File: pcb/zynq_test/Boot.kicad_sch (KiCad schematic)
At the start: 10 parts, among them J901 A-MicroTF-1.85A, U902 MT25QL01GBBB8ESF-0SIT, U903 TXS02612RTW

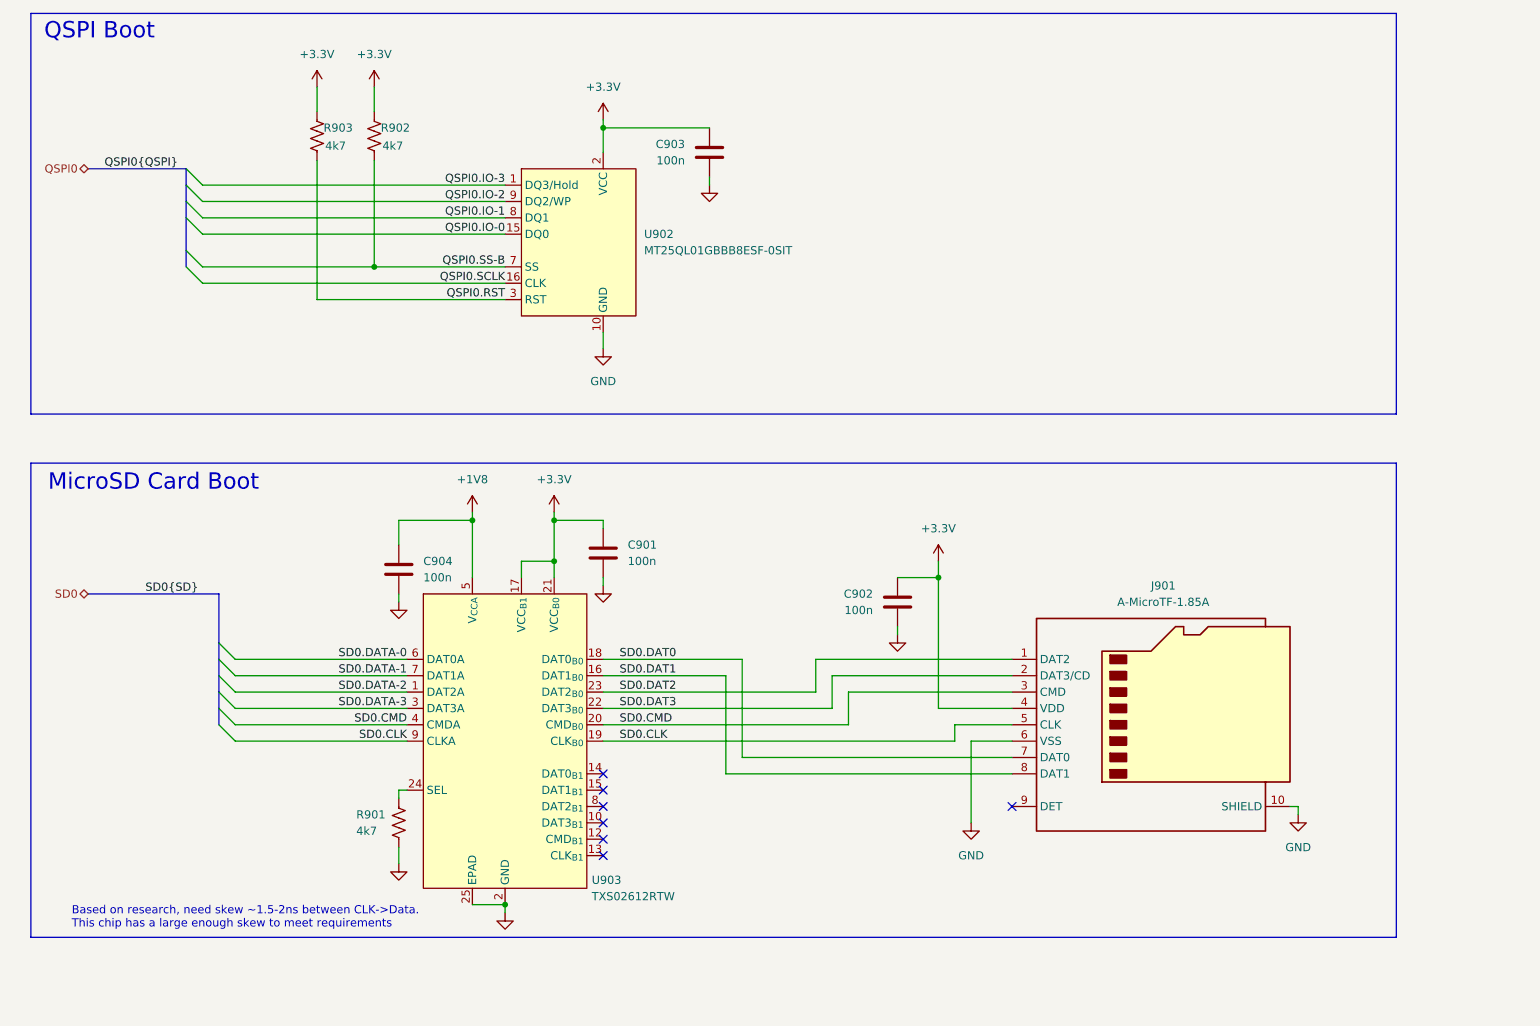
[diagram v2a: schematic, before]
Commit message: Connected DDR3, cleaned up some thing
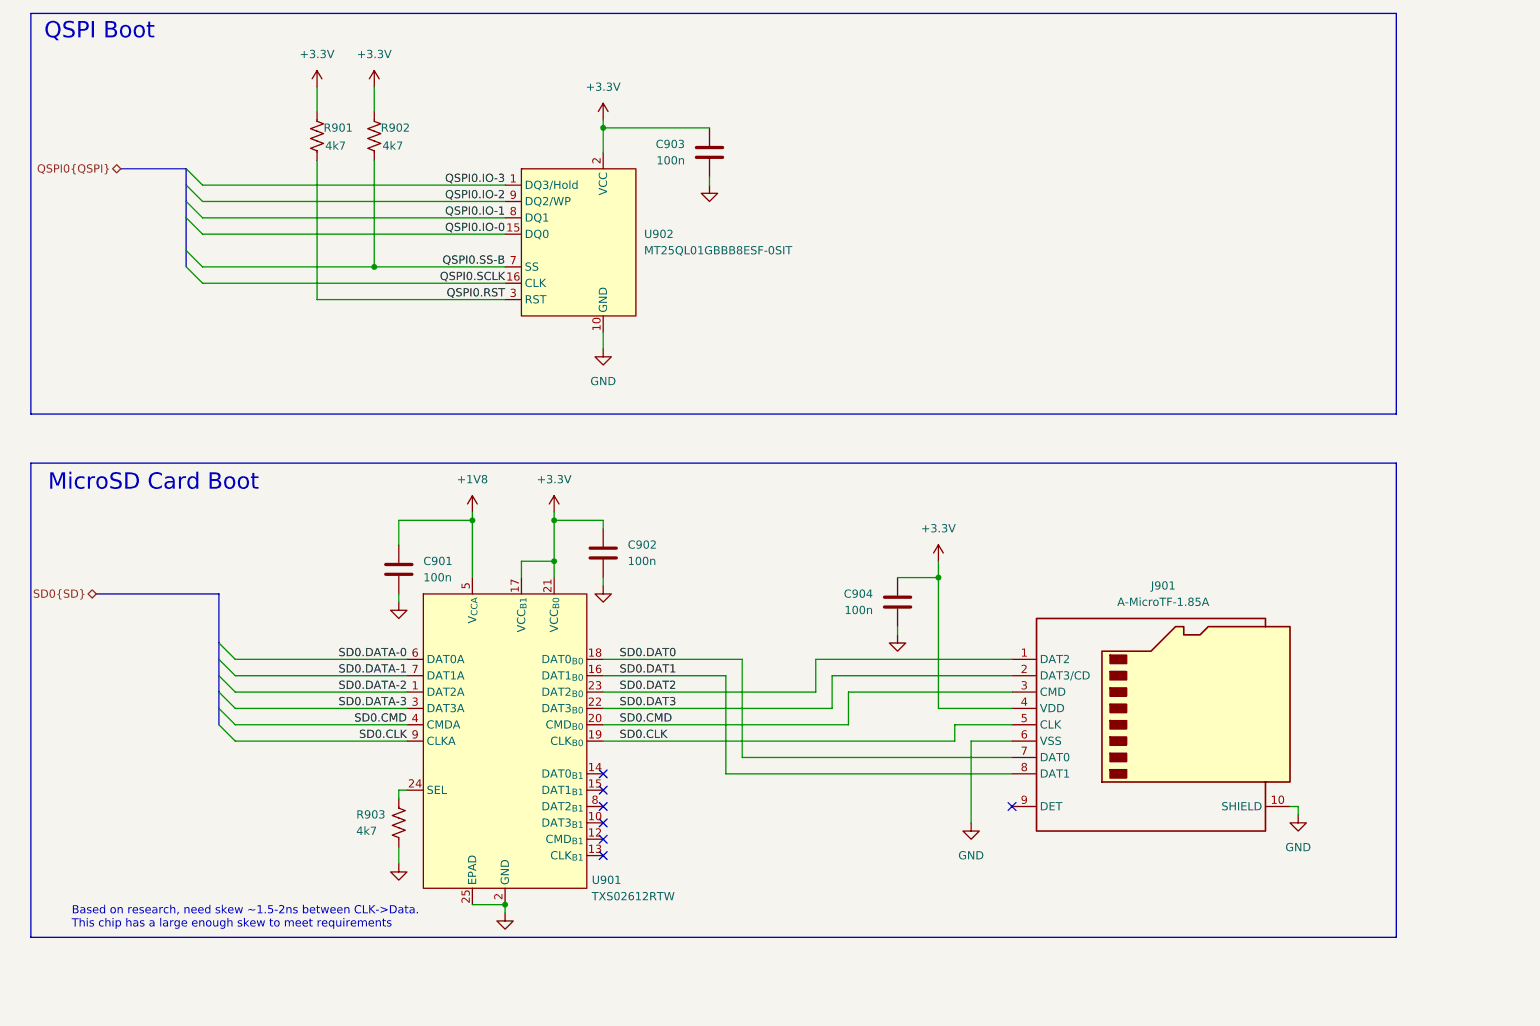
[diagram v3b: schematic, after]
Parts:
- U901: renamed from U903; footprint Package_DFN_QFN:WQFN-24-1EP_4x4mm_P0.5mm_EP2.45x2.45mm -> Package_DFN_QFN:WQFN-24-1EP_4x4mm_P0.5mm_EP2.45x2.45mm_ThermalVias
- renumbered C904 to C901, C901 to C902, C902 to C904, R903 to R901, R901 to R903
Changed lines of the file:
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@@
 	(generator_version "9.0")
 	(paper "A4")
+	(title_block
+		(date "2025-09-06")
+		(rev "v1.0")
+	)
 	(rectangle
 		(start 30.48 21.59)
@@
 	(bus
 		(pts
-			(xy 39.37 45.72) (xy 54.61 45.72)
+			(xy 44.45 45.72) (xy 54.61 45.72)
 		)
 		(stroke
@@
 	(bus
 		(pts
-			(xy 39.37 111.76) (xy 59.69 111.76)
+			(xy 40.64 111.76) (xy 59.69 111.76)
 		)
 		(stroke
@@
 		)
 	)
-	(label "SD0{SD}"
-		(at 48.26 111.76 0)
-		(effects
-			(font
-				(size 1.27 1.27)
-			)
-			(justify left bottom)
-		)
-	)
 	(label "QSPI0.SCLK"
 		(at 104.14 63.5 180)
@@
 		)
 	)
-	(label "QSPI0{QSPI}"
-		(at 41.91 45.72 0)
-		(effects
-			(font
-				(size 1.27 1.27)
-			)
-			(justify left bottom)
-		)
-	)
 	(label "QSPI0.RST"
 		(at 104.14 66.04 180)
@@
 		)
 	)
-	(hierarchical_label "QSPI0"
+	(hierarchical_label "QSPI0{QSPI}"
 		(shape bidirectional)
-		(at 39.37 45.72 180)
+		(at 44.45 45.72 180)
 		(effects
 			(font
@@
 		)
 	)
-	(hierarchical_label "SD0"
+	(hierarchical_label "SD0{SD}"
 		(shape bidirectional)
-		(at 39.37 111.76 180)
+		(at 40.64 111.76 180)
 		(effects
 			(font
@@
 		(dnp no)
 		(fields_autoplaced yes)
-		(property "Reference" "#PWR0912"
+		(property "Reference" "#PWR0901"
 			(at 74.93 36.83 0)
 			(effects
@@
 			(project "zynq_test"
 				(path "/0637578d-4ce5-4d31-b973-2de977269ea5/054c8c8d-10fe-458e-89fa-3861c8d6d3b7"
-					(reference "#PWR0912")
+					(reference "#PWR0901")
 					(unit 1)
 				)
@@
 		(dnp no)
 		(fields_autoplaced yes)
-		(property "Reference" "#PWR0908"
+		(property "Reference" "#PWR0912"
 			(at 165.1 124.46 0)
 			(effects
@@
 			(project "zynq_test"
 				(path "/0637578d-4ce5-4d31-b973-2de977269ea5/054c8c8d-10fe-458e-89fa-3861c8d6d3b7"
-					(reference "#PWR0908")
+					(reference "#PWR0912")
 					(unit 1)
 				)
@@
 		(dnp no)
 		(fields_autoplaced yes)
-		(property "Reference" "#PWR0913"
+		(property "Reference" "#PWR0911"
 			(at 135.89 54.61 0)
 			(effects
@@
 			(project "zynq_test"
 				(path "/0637578d-4ce5-4d31-b973-2de977269ea5/054c8c8d-10fe-458e-89fa-3861c8d6d3b7"
-					(reference "#PWR0913")
+					(reference "#PWR0911")
 					(unit 1)
 				)
@@
 		(on_board yes)
 		(dnp no)
-		(property "Reference" "R903"
+		(property "Reference" "R901"
 			(at 75.946 39.37 0)
 			(effects
@@
 			(project "zynq_test"
 				(path "/0637578d-4ce5-4d31-b973-2de977269ea5/054c8c8d-10fe-458e-89fa-3861c8d6d3b7"
-					(reference "R903")
+					(reference "R901")
 					(unit 1)
 				)
@@
 		(dnp no)
 		(fields_autoplaced yes)
-		(property "Reference" "#PWR0915"
+		(property "Reference" "#PWR0904"
 			(at 87.63 160.02 0)
 			(effects
@@
 			(project "zynq_test"
 				(path "/0637578d-4ce5-4d31-b973-2de977269ea5/054c8c8d-10fe-458e-89fa-3861c8d6d3b7"
-					(reference "#PWR0915")
+					(reference "#PWR0904")
 					(unit 1)
 				)
@@
 		(dnp no)
 		(fields_autoplaced yes)
-		(property "Reference" "#PWR0903"
+		(property "Reference" "#PWR0913"
 			(at 171.45 110.49 0)
 			(effects
@@
 			(project "zynq_test"
 				(path "/0637578d-4ce5-4d31-b973-2de977269ea5/054c8c8d-10fe-458e-89fa-3861c8d6d3b7"
-					(reference "#PWR0903")
+					(reference "#PWR0913")
 					(unit 1)
 				)
@@
 		(dnp no)
 		(fields_autoplaced yes)
-		(property "Reference" "#PWR0906"
+		(property "Reference" "#PWR0903"
 			(at 87.63 119.38 0)
 			(effects
@@
 			(project "zynq_test"
 				(path "/0637578d-4ce5-4d31-b973-2de977269ea5/054c8c8d-10fe-458e-89fa-3861c8d6d3b7"
-					(reference "#PWR0906")
+					(reference "#PWR0903")
 					(unit 1)
 				)
@@
 		(dnp no)
 		(fields_autoplaced yes)
-		(property "Reference" "#PWR0904"
+		(property "Reference" "#PWR0914"
 			(at 176.53 153.67 0)
 			(effects
@@
 			(project "zynq_test"
 				(path "/0637578d-4ce5-4d31-b973-2de977269ea5/054c8c8d-10fe-458e-89fa-3861c8d6d3b7"
-					(reference "#PWR0904")
+					(reference "#PWR0914")
 					(unit 1)
 				)
@@
 		(on_board yes)
 		(dnp no)
-		(property "Reference" "U903"
+		(property "Reference" "U901"
 			(at 117.602 156.21 0)
 			(effects
@@
 			)
 		)
-		(property "Footprint" "Package_DFN_QFN:WQFN-24-1EP_4x4mm_P0.5mm_EP2.45x2.45mm"
+		(property "Footprint" "Package_DFN_QFN:WQFN-24-1EP_4x4mm_P0.5mm_EP2.45x2.45mm_ThermalVias"
 			(at 104.14 170.18 0)
 			(effects
@@
 			(project ""
 				(path "/0637578d-4ce5-4d31-b973-2de977269ea5/054c8c8d-10fe-458e-89fa-3861c8d6d3b7"
-					(reference "U903")
+					(reference "U901")
 					(unit 1)
 				)
@@
 		(on_board yes)
 		(dnp no)
-		(property "Reference" "R901"
+		(property "Reference" "R903"
 			(at 81.026 146.05 0)
 			(effects
@@
 			(project ""
 				(path "/0637578d-4ce5-4d31-b973-2de977269ea5/054c8c8d-10fe-458e-89fa-3861c8d6d3b7"
-					(reference "R901")
+					(reference "R903")
 					(unit 1)
 				)
@@
 		(dnp no)
 		(fields_autoplaced yes)
-		(property "Reference" "C902"
+		(property "Reference" "C904"
 			(at 161.29 111.7599 0)
 			(effects
@@
 			(project "zynq_test"
 				(path "/0637578d-4ce5-4d31-b973-2de977269ea5/054c8c8d-10fe-458e-89fa-3861c8d6d3b7"
-					(reference "C902")
+					(reference "C904")
 					(unit 1)
 				)
@@
 		(dnp no)
 		(fields_autoplaced yes)
-		(property "Reference" "C901"
+		(property "Reference" "C902"
 			(at 123.19 104.1399 0)
 			(effects
@@
 			(project ""
 				(path "/0637578d-4ce5-4d31-b973-2de977269ea5/054c8c8d-10fe-458e-89fa-3861c8d6d3b7"
-					(reference "C901")
+					(reference "C902")
 					(unit 1)
 				)
@@
 		(dnp no)
 		(fields_autoplaced yes)
-		(property "Reference" "#PWR0907"
+		(property "Reference" "#PWR0910"
 			(at 119.38 116.84 0)
 			(effects
@@
 			(project "zynq_test"
 				(path "/0637578d-4ce5-4d31-b973-2de977269ea5/054c8c8d-10fe-458e-89fa-3861c8d6d3b7"
-					(reference "#PWR0907")
+					(reference "#PWR0910")
 					(unit 1)
 				)
@@
 		(dnp no)
 		(fields_autoplaced yes)
-		(property "Reference" "#PWR0910"
+		(property "Reference" "#PWR0902"
 			(at 83.82 36.83 0)
 			(effects
@@
 			(project "zynq_test"
 				(path "/0637578d-4ce5-4d31-b973-2de977269ea5/054c8c8d-10fe-458e-89fa-3861c8d6d3b7"
-					(reference "#PWR0910")
+					(reference "#PWR0902")
 					(unit 1)
 				)
@@
 		(dnp no)
 		(fields_autoplaced yes)
-		(property "Reference" "#PWR0901"
+		(property "Reference" "#PWR0915"
 			(at 227.33 152.4 0)
 			(effects
@@
 			(project ""
 				(path "/0637578d-4ce5-4d31-b973-2de977269ea5/054c8c8d-10fe-458e-89fa-3861c8d6d3b7"
-					(reference "#PWR0901")
+					(reference "#PWR0915")
 					(unit 1)
 				)
@@
 		(dnp no)
 		(fields_autoplaced yes)
-		(property "Reference" "#PWR0909"
+		(property "Reference" "#PWR0908"
 			(at 119.38 41.91 0)
 			(effects
@@
 			(project "zynq_test"
 				(path "/0637578d-4ce5-4d31-b973-2de977269ea5/054c8c8d-10fe-458e-89fa-3861c8d6d3b7"
-					(reference "#PWR0909")
+					(reference "#PWR0908")
 					(unit 1)
 				)
@@
 		(dnp no)
 		(fields_autoplaced yes)
-		(property "Reference" "C904"
+		(property "Reference" "C901"
 			(at 91.44 106.6799 0)
 			(effects
@@
 			(project "zynq_test"
 				(path "/0637578d-4ce5-4d31-b973-2de977269ea5/054c8c8d-10fe-458e-89fa-3861c8d6d3b7"
-					(reference "C904")
+					(reference "C901")
 					(unit 1)
 				)
@@
 		(dnp no)
 		(fields_autoplaced yes)
-		(property "Reference" "#PWR0902"
+		(property "Reference" "#PWR0907"
 			(at 111.76 102.87 0)
 			(effects
@@
 			(project ""
 				(path "/0637578d-4ce5-4d31-b973-2de977269ea5/054c8c8d-10fe-458e-89fa-3861c8d6d3b7"
-					(reference "#PWR0902")
+					(reference "#PWR0907")
 					(unit 1)
 				)
@@
 		(dnp no)
 		(fields_autoplaced yes)
-		(property "Reference" "#PWR0911"
+		(property "Reference" "#PWR0909"
 			(at 119.38 80.01 0)
 			(effects
@@
 			(project "zynq_test"
 				(path "/0637578d-4ce5-4d31-b973-2de977269ea5/054c8c8d-10fe-458e-89fa-3861c8d6d3b7"
-					(reference "#PWR0911")
+					(reference "#PWR0909")
 					(unit 1)
 				)
@@
 		(dnp no)
 		(fields_autoplaced yes)
-		(property "Reference" "#PWR0914"
+		(property "Reference" "#PWR0906"
 			(at 104.14 167.64 0)
 			(effects
@@
 			(project "zynq_test"
 				(path "/0637578d-4ce5-4d31-b973-2de977269ea5/054c8c8d-10fe-458e-89fa-3861c8d6d3b7"
-					(reference "#PWR0914")
+					(reference "#PWR0906")
 					(unit 1)
 				)

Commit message: Finished Power Supply
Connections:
- net +3.3V renamed +3V3
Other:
- title: (none) -> Boot
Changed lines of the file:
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@@
 	(paper "A4")
 	(title_block
-		(date "2025-09-06")
-		(rev "v1.0")
+		(title "Boot")
+		(date "2025-09-13")
+		(rev "A")
 	)
 	(rectangle
@@
 			)
 		)
-		(property "Value" "+3.3V"
+		(property "Value" "+3V3"
 			(at 74.93 27.94 0)
 			(effects
@@
 			)
 		)
-		(property "Value" "+3.3V"
+		(property "Value" "+3V3"
 			(at 171.45 101.6 0)
 			(effects
@@
 			)
 		)
-		(property "Value" "+3.3V"
+		(property "Value" "+3V3"
 			(at 83.82 27.94 0)
 			(effects
@@
 			)
 		)
-		(property "Value" "+3.3V"
+		(property "Value" "+3V3"
 			(at 119.38 33.02 0)
 			(effects
@@
 			)
 		)
-		(property "Value" "+3.3V"
+		(property "Value" "+3V3"
 			(at 111.76 93.98 0)
 			(effects

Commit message: Finished most of the schematic, will start routing soon
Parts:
- U901: footprint Package_DFN_QFN:WQFN-24-1EP_4x4mm_P0.5mm_EP2.45x2.45mm_ThermalVias -> Package_DFN_QFN:WQFN-24-1EP_4x4mm_P0.5mm_EP2.45x2.45mm
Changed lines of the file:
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@@
 			)
 		)
-		(property "Footprint" "Package_DFN_QFN:WQFN-24-1EP_4x4mm_P0.5mm_EP2.45x2.45mm_ThermalVias"
+		(property "Footprint" "Package_DFN_QFN:WQFN-24-1EP_4x4mm_P0.5mm_EP2.45x2.45mm"
 			(at 104.14 170.18 0)
 			(effects

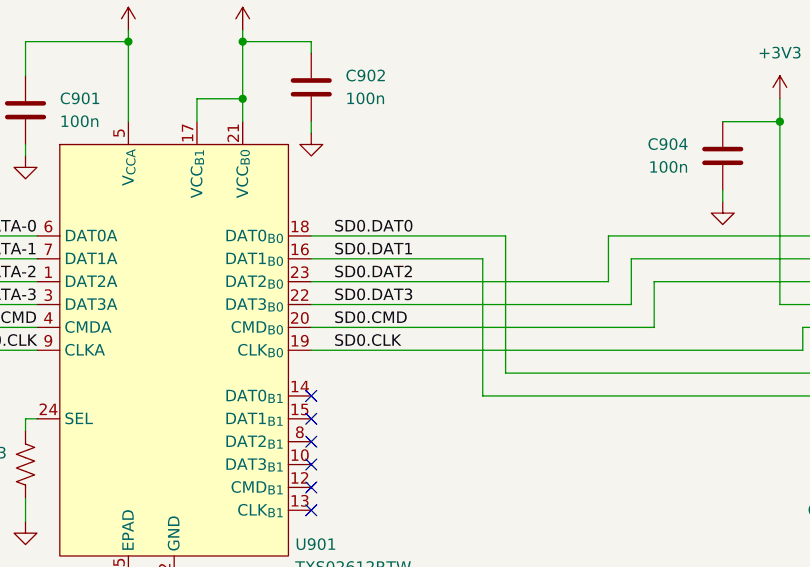
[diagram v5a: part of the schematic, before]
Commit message: finished diff of HDMI
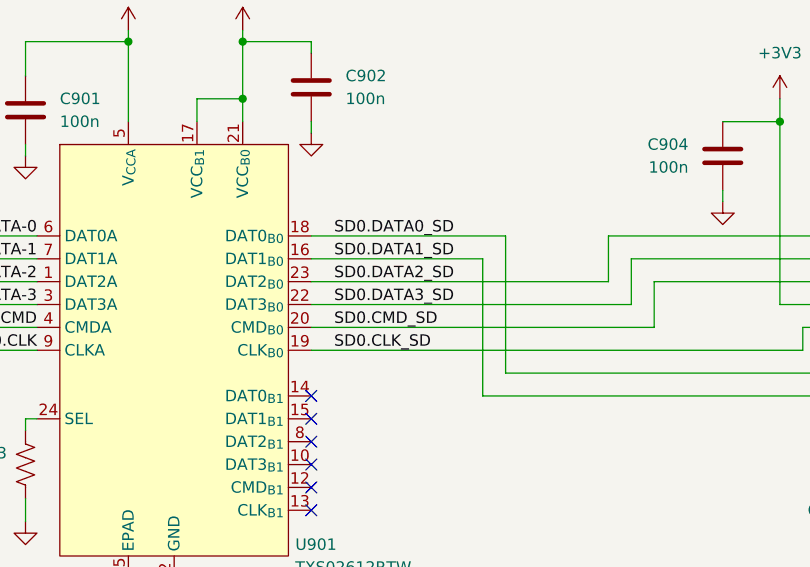
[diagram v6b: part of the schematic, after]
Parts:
- R901, R902: footprint (none) -> Resistor_SMD:R_0402_1005Metric
- U902: footprint (none) -> Package_SO:SOIC-16W_7.5x10.3mm_P1.27mm
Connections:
- net SD0.CLK: no longer J901.5 (CLK), U901.19 (CLK_{B0})
- net SD0.CMD: no longer J901.3 (CMD), U901.20 (CMD_{B0})
- net SD0.DAT0 renamed SD0.DATA0_SD
- net SD0.DAT1 renamed SD0.DATA1_SD
- net SD0.DAT2 renamed SD0.DATA2_SD
- net SD0.DAT3 renamed SD0.DATA3_SD
- new net SD0.CLK_SD: J901.5 (CLK), U901.19 (CLK_{B0})
- new net SD0.CMD_SD: J901.3 (CMD), U901.20 (CMD_{B0})
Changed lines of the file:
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@@
 		)
 	)
-	(label "SD0.DAT2"
+	(label "SD0.DATA2_SD"
 		(at 121.92 127 0)
 		(effects
@@
 		)
 	)
-	(label "SD0.CMD"
+	(label "SD0.CMD_SD"
 		(at 121.92 132.08 0)
 		(effects
@@
 		)
 	)
-	(label "SD0.CLK"
+	(label "SD0.CLK_SD"
 		(at 121.92 134.62 0)
 		(effects
@@
 		)
 	)
-	(label "SD0.DAT3"
+	(label "SD0.DATA3_SD"
 		(at 121.92 129.54 0)
 		(effects
@@
 		)
 	)
-	(label "SD0.DAT0"
+	(label "SD0.DATA0_SD"
 		(at 121.92 121.92 0)
 		(effects
@@
 		)
 	)
-	(label "SD0.DAT1"
+	(label "SD0.DATA1_SD"
 		(at 121.92 124.46 0)
 		(effects
@@
 			)
 		)
-		(property "Footprint" ""
+		(property "Footprint" "Resistor_SMD:R_0402_1005Metric"
 			(at 84.836 40.894 90)
 			(effects
@@
 			)
 		)
-		(property "Footprint" ""
+		(property "Footprint" "Resistor_SMD:R_0402_1005Metric"
 			(at 75.946 40.894 90)
 			(effects
@@
 			)
 		)
-		(property "Footprint" ""
+		(property "Footprint" "Package_SO:SOIC-16W_7.5x10.3mm_P1.27mm"
 			(at 115.57 45.72 0)
 			(effects

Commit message: Almost done with BOM
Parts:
- C901, C902, C903, C904: footprint (none) -> Capacitor_SMD:C_0402_1005Metric
- R903: footprint (none) -> Resistor_SMD:R_0402_1005Metric
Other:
- moved on the sheet: C901, C902, C904, J901, R903, U901

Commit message: Version sent to JLCPCB
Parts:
- added R904, R905, R906, R907, R908: 10k, Resistor_SMD:R_0402_1005Metric, symbol Device:R_US
- C901, C902, C903, C904: JLCPCB Part# (none) -> C1525; PART_NUMBER (none) -> CL05B104KO5NNNC
- J901: JLCPCB Part# (none) -> C22467599; PART_NUMBER (none) -> A-MicroTF-1.85A
- R901, R902, R903: JLCPCB Part# (none) -> C327817; PART_NUMBER (none) -> MR04X4701FTL
- U901: JLCPCB Part# (none) -> C140276; PART_NUMBER (none) -> TXS02612RTWR
- U902: JLCPCB Part# (none) -> C2061920; PART_NUMBER (none) -> MT25QL01GBBB8ESF-0SIT
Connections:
- net +3V3: now also R904.2, R905.2, R906.2, R907.2, R908.2
- net SD0.CMD_SD: now also R906.1
- net SD0.DATA0_SD: now also R907.1
- net SD0.DATA1_SD: now also R908.1
- net SD0.DATA2_SD: now also R904.1
- net SD0.DATA3_SD: now also R905.1
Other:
- note added: "1 Gbit (128MB)"
- moved on the sheet: C904, J901
